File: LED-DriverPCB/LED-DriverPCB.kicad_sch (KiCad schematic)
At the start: 51 parts, among them J1 Screw_Terminal_01x03, J12 Screw_Terminal_01x02, J13 Screw_Terminal_01x02, J14 Screw_Terminal_01x02, J15 Screw_Terminal_01x02, J16 Screw_Terminal_01x02, J17 Screw_Terminal_01x02, J18 Screw_Terminal_01x02, J19 Screw_Terminal_01x02, J2 Screw_Terminal_01x03, J20 Conn_ARM_SWD_TagConnect_TC2030, J3 Screw_Terminal_01x03, J4 Screw_Terminal_01x03, J5 Screw_Terminal_01x03, J6 Screw_Terminal_01x03, J7 Screw_Terminal_01x03, J8 Screw_Terminal_01x03, J9 USB_C_Receptacle_USB2.0_16P, U1 STM32F103RCTx, U2 TXB0108PW, U3 AMS1117-3.3, U4 USBLC6-2SC6, X1 8MHz

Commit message: Finished PCB
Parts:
- added D1: LED, LED_SMD:LED_0603_1608Metric, symbol Device:LED
- added R6: 1k, Resistor_SMD:R_0402_1005Metric, symbol Device:R
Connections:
- net +3.3V: now also D1.2 (A)
- net GND: now also R6.2
- new net: D1.1 (K), R6.1
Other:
- moved on the sheet: C11, C12

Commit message: Created manufaturing files
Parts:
- U4: JLCPCB Part # USBLC6-2SC6 -> C7519
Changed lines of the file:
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@@
 			)
 		)
-		(property "JLCPCB Part #" "USBLC6-2SC6"
+		(property "JLCPCB Part #" "C7519"
 			(at 189.23 69.85 0)
 			(effects

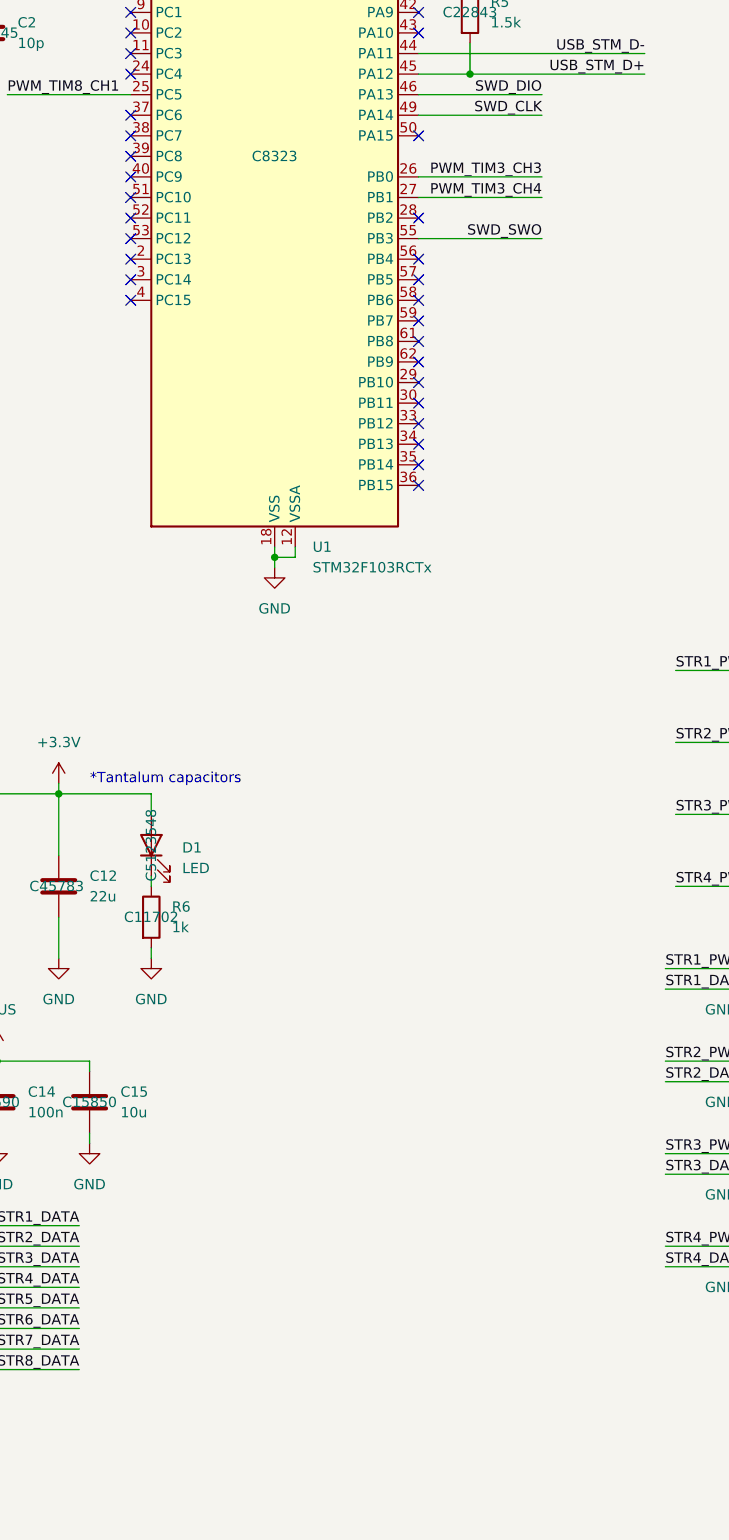
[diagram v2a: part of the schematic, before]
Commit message: Changed MCU and level shifter
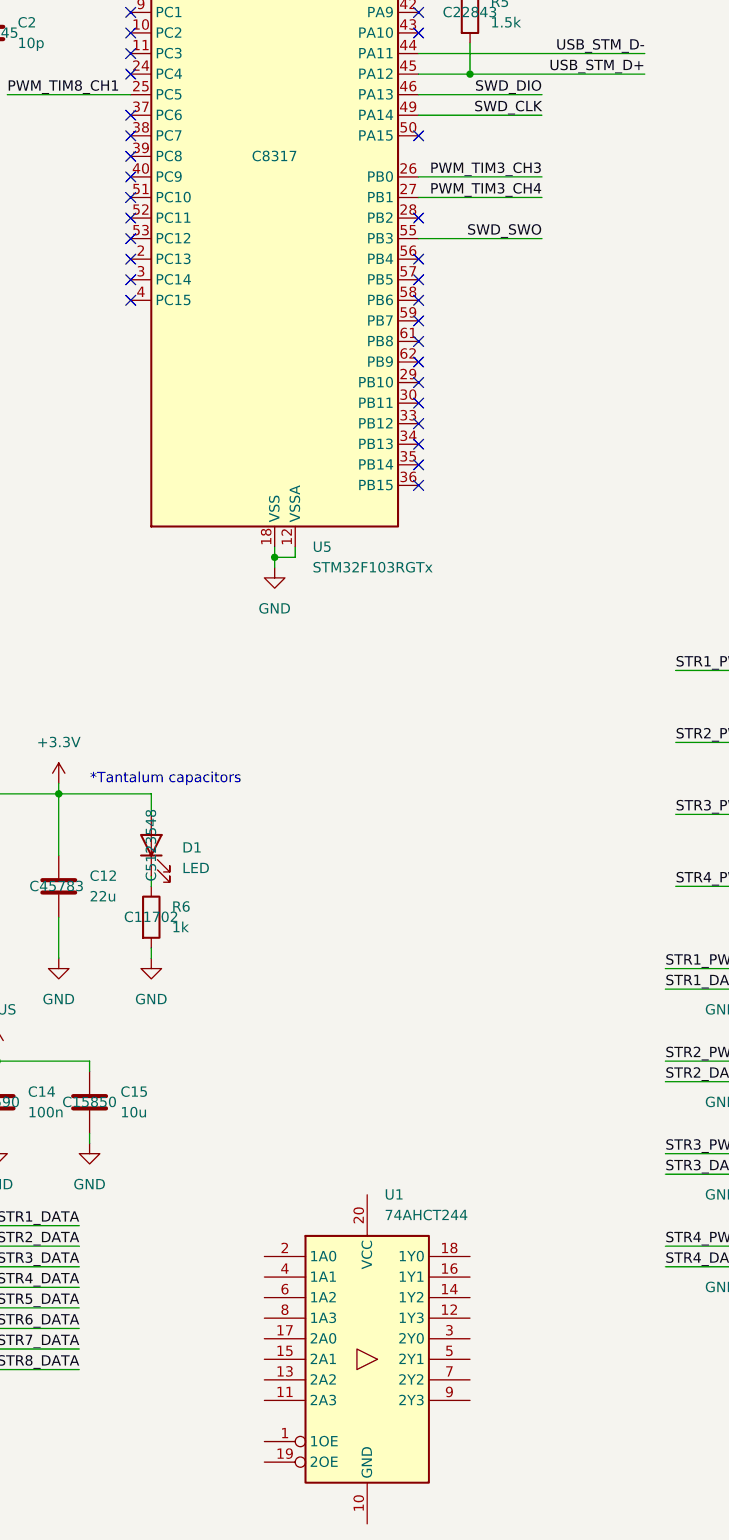
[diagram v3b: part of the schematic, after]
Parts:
- removed U1: STM32F103RCTx, Package_QFP:LQFP-64_10x10mm_P0.5mm, symbol MCU_ST_STM32F1:STM32F103RCTx
- added U1: 74AHCT244, symbol 74xx:74AHCT244
- added U5: STM32F103RGTx, Package_QFP:LQFP-64_10x10mm_P0.5mm, symbol MCU_ST_STM32F1:STM32F103RGTx
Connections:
- net +3.3V: now also U5.1 (VBAT), U5.13 (VDDA), U5.19 (VDD), U5.32 (VDD), U5.48 (VDD), U5.64 (VDD)
- net BOOT: now also U5.60 (BOOT0)
- net GND: now also U5.12 (VSSA), U5.18 (VSS), U5.31 (VSS), U5.47 (VSS), U5.63 (VSS)
- net HSE_IN: now also U5.5 (PD0)
- net HSE_OUT: now also U5.6 (PD1)
- net PWM_TIM3_CH1: now also U5.22 (PA6)
- net PWM_TIM3_CH3: now also U5.26 (PB0)
- net PWM_TIM3_CH4: now also U5.27 (PB1)
- net PWM_TIM5_CH1: now also U5.14 (PA0)
- net PWM_TIM5_CH2: now also U5.15 (PA1)
- net PWM_TIM5_CH3: now also U5.16 (PA2)
- net PWM_TIM5_CH4: now also U5.17 (PA3)
- net PWM_TIM8_CH1: now also U5.25 (PC5)
- net SWD_CLK: now also U5.49 (PA14)
- net SWD_DIO: now also U5.46 (PA13)
- net SWD_NRST: now also U5.7 (NRST)
- net SWD_SWO: now also U5.55 (PB3)
- net USB_STM_D+: now also U5.45 (PA12)
- net USB_STM_D-: now also U5.44 (PA11)

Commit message: Added schematic for new level shifter
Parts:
- removed C13, C14: 100n, Capacitor_SMD:C_0603_1608Metric, symbol Device:C
- removed C15: 10u, Capacitor_SMD:C_0805_2012Metric, symbol Device:C
- removed U2: TXB0108PW, Package_SO:TSSOP-20_4.4x6.5mm_P0.65mm, symbol Logic_LevelTranslator:TXB0108PW
- added C16: 100n, symbol Device:C
- added R10, R11, R12, R13, R14, R15, R8, R9: 0R, symbol Device:R
- added R7: 10k, symbol Device:R
- added TP1, TP2, TP3, TP4, TP5, TP6, TP7, TP8: TestPoint, symbol Connector:TestPoint
- R4: value 50k -> 10k; footprint Resistor_SMD:R_0603_1608Metric -> (none); JLCPCB Part # C861451 -> (none)
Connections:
- net SHIFTER_OE is gone; now on net GND: R4.2
- net +3.3V: no longer R4.1
- net GND: now also U1.10 (GND), C16.2, R7.2
- net PWM_TIM3_CH1: now also U1.17 (2A0), TP5.1
- net PWM_TIM3_CH3: now also U1.15 (2A1), TP6.1
- net PWM_TIM3_CH4: now also U1.13 (2A2), TP7.1
- net PWM_TIM5_CH1: now also U1.2 (1A0), TP1.1
- net PWM_TIM5_CH2: now also U1.4 (1A1), TP2.1
- net PWM_TIM5_CH3: now also U1.6 (1A2), TP3.1
- net PWM_TIM5_CH4: now also U1.8 (1A3), TP4.1
- net PWM_TIM8_CH1: now also U1.11 (2A3), TP8.1
- net STR1_DATA: now also R8.2
- net STR2_DATA: now also R9.1
- net STR3_DATA: now also R10.2
- net STR4_DATA: now also R11.2
- net STR5_DATA: now also R12.2
- net STR6_DATA: now also R13.2
- net STR7_DATA: now also R14.2
- net STR8_DATA: now also R15.2
- net VBUS: now also U1.20 (VCC), C16.1
- net at U1.1 (1OE): now also R4.1
- net at U1.12 (1Y3): now also R11.1
- net at U1.14 (1Y2): now also R10.1
- net at U1.16 (1Y1): now also R9.2
- net at U1.18 (1Y0): now also R8.1
- net at U1.19 (2OE): now also R7.1
- net at U1.3 (2Y0): now also R12.1
- net at U1.5 (2Y1): now also R13.1
- net at U1.7 (2Y2): now also R14.1
- net at U1.9 (2Y3): now also R15.1
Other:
- moved on the sheet: J1, J12, J13, J14, J15, J16, J17, J18, J19, J2, J3, J4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

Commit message: fixed bugs
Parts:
- C16: footprint (none) -> Capacitor_SMD:C_0603_1608Metric
- R10, R11, R12, R13, R14, R15, R4, R7, R8, R9: footprint (none) -> Resistor_SMD:R_0603_1608Metric
- TP1, TP2, TP3, TP4: footprint (none) -> TestPoint:TestPoint_Pad_1.0x1.0mm
- TP5: renamed from TP8; footprint (none) -> TestPoint:TestPoint_Pad_1.0x1.0mm
- TP6: renamed from TP7; footprint (none) -> TestPoint:TestPoint_Pad_1.0x1.0mm
- TP7: renamed from TP6; footprint (none) -> TestPoint:TestPoint_Pad_1.0x1.0mm
- TP8: renamed from TP5; footprint (none) -> TestPoint:TestPoint_Pad_1.0x1.0mm
- U1: footprint (none) -> Package_SO:TSSOP-20_4.4x6.5mm_P0.65mm
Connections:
- net PWM_TIM3_CH1: now also U1.11 (2A3); no longer TP8.1, U1.17 (2A0)
- net PWM_TIM3_CH3: no longer TP7.1
- net PWM_TIM3_CH4: now also U1.17 (2A0); no longer TP6.1, U1.13 (2A2)
- net PWM_TIM5_CH1: no longer TP1.1
- net PWM_TIM5_CH2: no longer TP2.1
- net PWM_TIM5_CH3: no longer TP3.1
- net PWM_TIM5_CH4: no longer TP4.1
- net PWM_TIM8_CH1: now also U1.13 (2A2), U5.37 (PC6); no longer TP5.1, U1.11 (2A3), U5.25 (PC5)
- net STR1_DATA: now also TP1.1
- net STR2_DATA: now also TP2.1
- net STR3_DATA: now also TP3.1
- net STR4_DATA: now also TP4.1
- net STR5_DATA: now also R15.2, TP5.1; no longer R12.2
- net STR6_DATA: now also R14.2, TP6.1; no longer R13.2
- net STR7_DATA: now also R13.2, TP7.1; no longer R14.2
- net STR8_DATA: now also R12.2, TP8.1; no longer R15.2
- net 1Y1_RES: now reaches R9.2, U1.16 (1Y1)
- net 1Y3_RES: now reaches R11.1, U1.12 (1Y3)
- net 1Y2_RES: now reaches R10.1, U1.14 (1Y2)
- net 1Y0_RES: now reaches R8.1, U1.18 (1Y0)
- net 2Y0_RES: now reaches R12.1, U1.3 (2Y0)
- net 2Y1_RES: now reaches R13.1, U1.5 (2Y1)
- net 2Y2_RES: now reaches R14.1, U1.7 (2Y2)
- net 2Y3_RES: now reaches R15.1, U1.9 (2Y3)
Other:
- moved on the sheet: C16, R10, R11, R12, R13, R14, R15, R4, R7, R8, R9, TP1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

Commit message: Small changes
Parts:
- C16: JLCPCB Part # (none) -> C1590
- R1: JLCPCB Part # C5184132 -> C25804
- R10, R11, R12, R13, R14, R15, R8, R9: JLCPCB Part # (none) -> C21189
- R4, R7: JLCPCB Part # (none) -> C25804
- U1: JLCPCB Part # (none) -> C484743
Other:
- note removed: "*Tantalum capacitors"
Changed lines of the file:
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@@
 		(company "Tim Short's Garage")
 	)
-	(text "*Tantalum capacitors"
-		(exclude_from_sim no)
-		(at 90.678 187.452 0)
-		(effects
-			(font
-				(size 1.27 1.27)
-			)
-		)
-	)
 	(text "LED-Driver PCB"
 		(exclude_from_sim no)
@@
 			)
 		)
+		(property "JLCPCB Part #" "C21189"
+			(at 200.66 210.82 0)
+			(effects
+				(font
+					(size 1.27 1.27)
+				)
+			)
+		)
 		(pin "2"
 		)
@@
 			)
 		)
+		(property "JLCPCB Part #" "C21189"
+			(at 200.66 218.44 0)
+			(effects
+				(font
+					(size 1.27 1.27)
+				)
+			)
+		)
 		(pin "1"
 		)
@@
 			)
 		)
-		(property "JLCPCB Part #" "C5184132"
+		(property "JLCPCB Part #" " C25804"
 			(at 73.66 74.93 0)
 			(effects
@@
 			)
 		)
+		(property "JLCPCB Part #" "C1590"
+			(at 180.34 195.58 0)
+			(effects
+				(font
+					(size 1.27 1.27)
+				)
+			)
+		)
 		(pin "1"
 		)
@@
 			)
 		)
+		(property "JLCPCB Part #" "C21189"
+			(at 200.66 213.36 0)
+			(effects
+				(font
+					(size 1.27 1.27)
+				)
+			)
+		)
 		(pin "2"
 		)
@@
 			)
 		)
+		(property "JLCPCB Part #" "C21189"
+			(at 200.66 215.9 0)
+			(effects
+				(font
+					(size 1.27 1.27)
+				)
+			)
+		)
 		(pin "1"
 		)
@@
 			)
 		)
+		(property "JLCPCB Part #" "C21189"
+			(at 200.66 226.06 0)
+			(effects
+				(font
+					(size 1.27 1.27)
+				)
+			)
+		)
 		(pin "1"
 		)
@@
 			)
 		)
+		(property "JLCPCB Part #" " C25804"
+			(at 142.24 240.03 0)
+			(effects
+				(font
+					(size 1.27 1.27)
+				)
+			)
+		)
 		(pin "1"
 		)
@@
 			)
 		)
+		(property "JLCPCB Part #" " C25804"
+			(at 132.08 240.03 0)
+			(effects
+				(font
+					(size 1.27 1.27)
+				)
+			)
+		)
 		(pin "1"
 		)
@@
 			)
 		)
+		(property "JLCPCB Part #" "C21189"
+			(at 200.66 208.28 0)
+			(effects
+				(font
+					(size 1.27 1.27)
+				)
+			)
+		)
 		(pin "1"
 		)
@@
 			)
 		)
+		(property "JLCPCB Part #" "C21189"
+			(at 200.66 223.52 0)
+			(effects
+				(font
+					(size 1.27 1.27)
+				)
+			)
+		)
 		(pin "2"
 		)
@@
 			)
 		)
+		(property "JLCPCB Part #" "C21189"
+			(at 200.66 220.98 0)
+			(effects
+				(font
+					(size 1.27 1.27)
+				)
+			)
+		)
 		(pin "1"
 		)
@@
 			)
 		)
+		(property "JLCPCB Part #" "C484743"
+			(at 165.1 220.98 0)
+			(effects
+				(font
+					(size 1.27 1.27)
+				)
+			)
+		)

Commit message: Fixed issues
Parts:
- renumbered TP8 to TP1, TP7 to TP2, TP6 to TP3, TP5 to TP4, TP4 to TP5, TP3 to TP6, TP2 to TP7, TP1 to TP8
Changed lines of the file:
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@@
 		(on_board yes)
 		(dnp no)
-		(property "Reference" "TP7"
+		(property "Reference" "TP2"
 			(at 223.52 217.17 0)
 			(effects
@@
 			(project "LED-DriverPCB"
 				(path "/f8915909-606a-4747-b712-208c2aaca226"
-					(reference "TP7")
+					(reference "TP2")
 					(unit 1)
 				)
@@
 		(on_board yes)
 		(dnp no)
-		(property "Reference" "TP2"
+		(property "Reference" "TP7"
 			(at 213.36 207.01 0)
 			(effects
@@
 			(project "LED-DriverPCB"
 				(path "/f8915909-606a-4747-b712-208c2aaca226"
-					(reference "TP2")
+					(reference "TP7")
 					(unit 1)
 				)
@@
 		(on_board yes)
 		(dnp no)
-		(property "Reference" "TP4"
+		(property "Reference" "TP5"
 			(at 218.44 212.09 0)
 			(effects
@@
 			(project "LED-DriverPCB"
 				(path "/f8915909-606a-4747-b712-208c2aaca226"
-					(reference "TP4")
+					(reference "TP5")
 					(unit 1)
 				)
@@
 		(on_board yes)
 		(dnp no)
-		(property "Reference" "TP5"
+		(property "Reference" "TP4"
 			(at 228.6 222.25 0)
 			(effects
@@
 			(project "LED-DriverPCB"
 				(path "/f8915909-606a-4747-b712-208c2aaca226"
-					(reference "TP5")
+					(reference "TP4")
 					(unit 1)
 				)
@@
 		(on_board yes)
 		(dnp no)
-		(property "Reference" "TP8"
+		(property "Reference" "TP1"
 			(at 220.98 214.63 0)
 			(effects
@@
 			(project "LED-DriverPCB"
 				(path "/f8915909-606a-4747-b712-208c2aaca226"
-					(reference "TP8")
+					(reference "TP1")
 					(unit 1)
 				)
@@
 		(on_board yes)
 		(dnp no)
-		(property "Reference" "TP3"
+		(property "Reference" "TP6"
 			(at 215.9 209.55 0)
 			(effects
@@
 			(project "LED-DriverPCB"
 				(path "/f8915909-606a-4747-b712-208c2aaca226"
-					(reference "TP3")
+					(reference "TP6")
 					(unit 1)
 				)
@@
 		(on_board yes)
 		(dnp no)
-		(property "Reference" "TP1"
+		(property "Reference" "TP8"
 			(at 210.82 204.47 0)
 			(effects
@@
 			(project ""
 				(path "/f8915909-606a-4747-b712-208c2aaca226"
-					(reference "TP1")
+					(reference "TP8")
 					(unit 1)
 				)
@@
 		(on_board yes)
 		(dnp no)
-		(property "Reference" "TP6"
+		(property "Reference" "TP3"
 			(at 226.06 219.71 0)
 			(effects
@@
 			(project "LED-DriverPCB"
 				(path "/f8915909-606a-4747-b712-208c2aaca226"
-					(reference "TP6")
+					(reference "TP3")
 					(unit 1)
 				)
